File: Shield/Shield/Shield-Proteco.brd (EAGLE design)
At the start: 106.3 x 81.3 mm, 46 parts

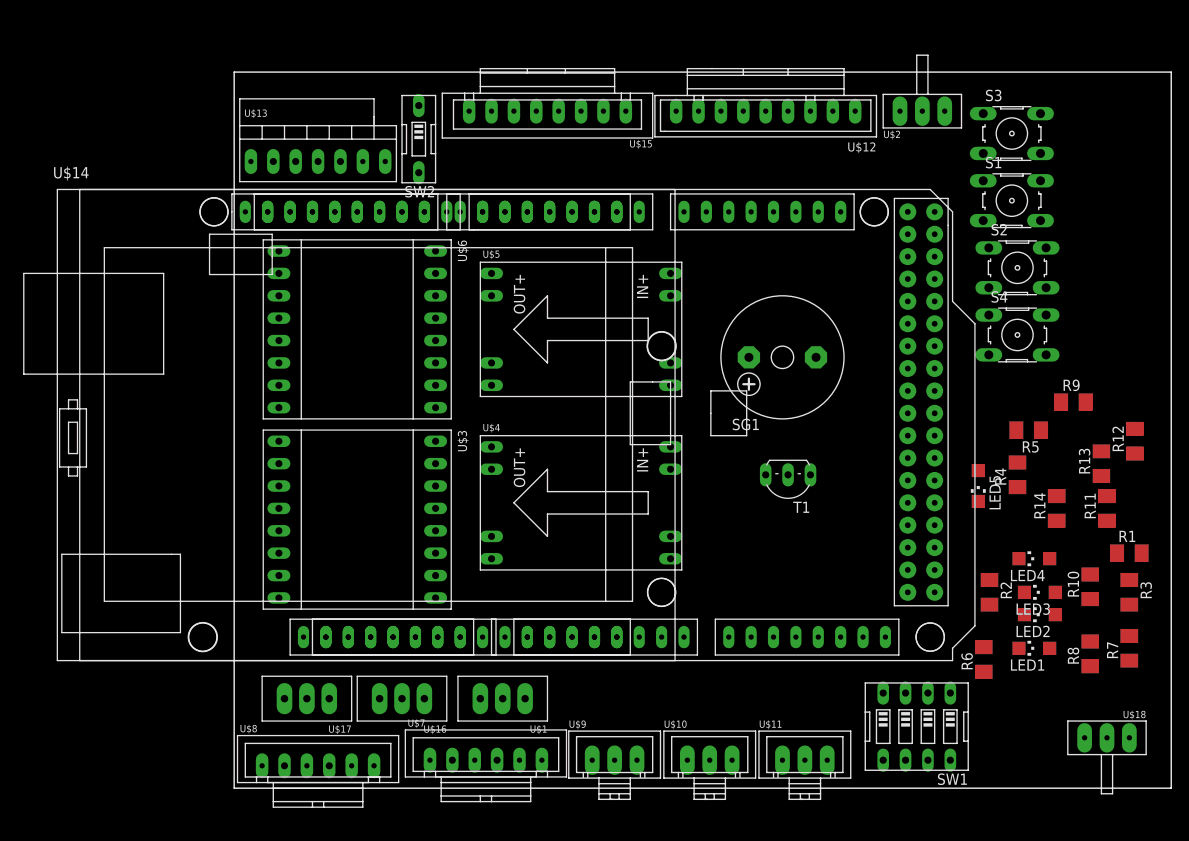
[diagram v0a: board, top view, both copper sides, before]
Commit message: Programacion Inalambrica con BT
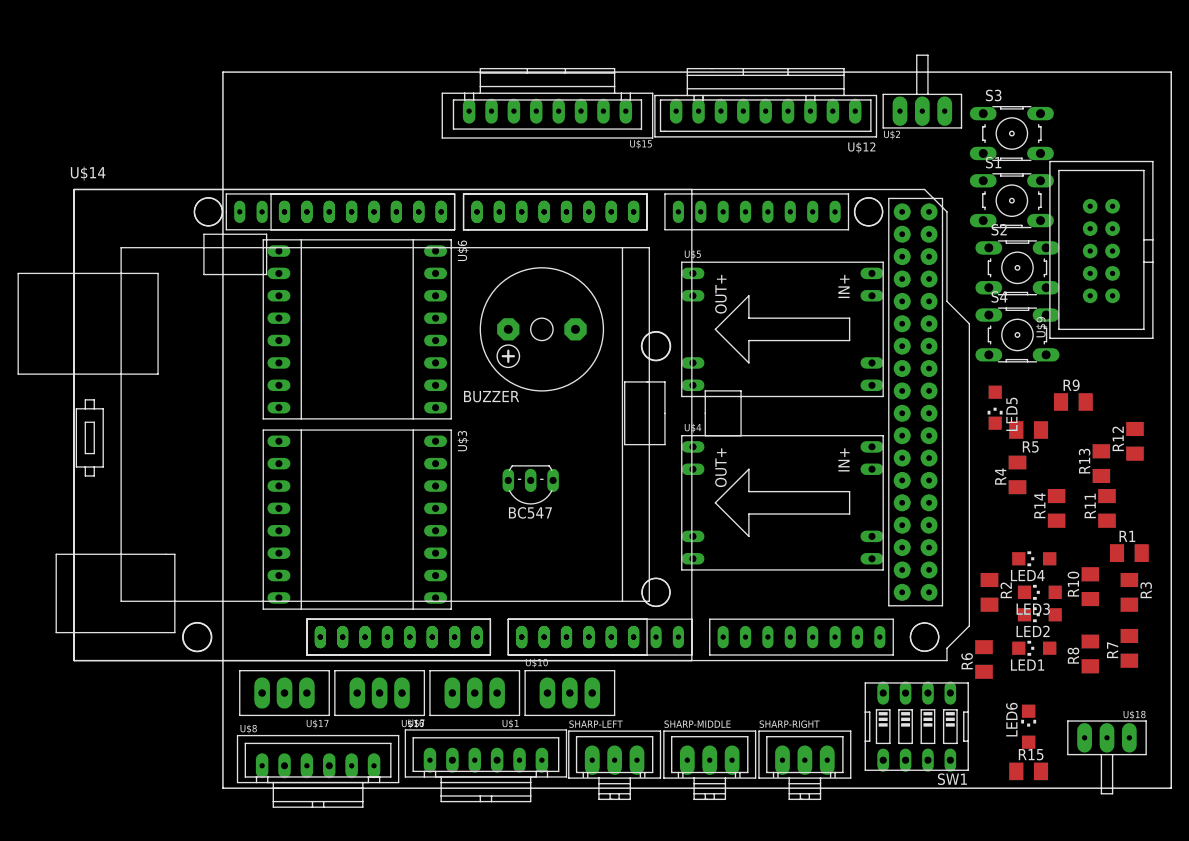
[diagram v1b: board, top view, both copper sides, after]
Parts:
- removed SG1: F/CM12P, buzzer:F/CM12P
- removed SW2: (no value), special:EDG-01
- removed T1: (no value), transistor:TO92-CBE
- removed U$13: HC-05-PROG, hc-xx:HC-05-PROG
- added BC547: (no value), transistor:TO92-CBE
- added BUZZER: F/CM12P, buzzer:F/CM12P
- added LED6: (no value), led:CHIPLED_1206
- added R15: (no value), rcl:M1206
- added SHARP-LEFT, SHARP-MIDDLE: SHARP, Sensores:SHARP
- U$10: value SHARP -> SERVOMOTORES; device Sensores:SHARP -> Motores:SERVO
- U$9: value SHARP -> SENSOR-MISCELANEOUS; device Sensores:SHARP -> Sensores:SENSOR-MISCELANEOUS
- moved U$9 79.9 mm to (98.4, 61.0), turned to 90 degrees
- moved U$4 22.9 mm to (62.2, 32.4)
- moved U$5 22.9 mm to (62.2, 52.1)
- moved U$10 17.6 mm to (38.1, 10.8)
- moved LED5 9.09 mm to (86.4, 43.2)
- moved U$1 3.24 mm to (27.3, 10.8)
- moved U$17 2.62 mm to (5.71, 10.8)
- moved U$16 2.62 mm to (16.5, 10.8)
- moved U$14 1.90 mm to (15.9, 38.7)
- moved ARDUINO-MEGA 0.64 mm to (31.1, 40.0)
- renumbered U$11 to SHARP-RIGHT
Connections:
- removed net N$16: SW2.1, U$13.RESET
- removed net RX0: U$13.RXD
- removed net TX0: U$13.TXD
- new net LED1: LED1.A
- new net LED2: LED2.A
- new net LED3: LED3.A
- new net LED4: LED4.A
- new net LED5: LED5.A
- new net N$100: U$3.AO2, U$3.BO2
- new net N$101: U$3.AO1, U$3.BO1
- new net N$102: U$7.OUTB
- new net N$103: U$7.OUTA
- new net N$104: U$7.M2
- new net N$105: U$7.M1
- new net N$106: U$8.OUTA
- new net N$107: U$8.OUTB
- new net N$108: U$8.M2
- new net N$109: U$8.M1
- new net N$110: U$9.3V3
- new net N$111: ARDUINO-MEGA.12
- new net N$112: ARDUINO-MEGA.11
- new net N$113: ARDUINO-MEGA.10
- new net N$114: ARDUINO-MEGA.9
- new net N$115: ARDUINO-MEGA.8
- new net N$116: ARDUINO-MEGA.7
- new net N$117: ARDUINO-MEGA.6
- new net N$69: U$9.1
- new net N$82: U$9.2
- new net N$83: U$9.3
- new net N$84: U$9.4
- new net N$85: U$9.5
- new net N$86: U$9.6
- new net N$87: U$9.7
- new net N$88: LED5.C, R14.2
- new net N$89: LED6.C, R15.2
- new net N$92: U$6.AI1, U$6.BI1
- new net N$93: U$6.AI2, U$6.BI2
- new net N$94: U$6.AO2, U$6.BO2
- new net N$95: U$6.AO1, U$6.BO1
- new net N$96: U$6.PWMA, U$6.PWMB
- new net N$97: U$3.AI1, U$3.BI1
- new net N$98: U$3.AI2, U$3.BI2
- new net N$99: U$3.PWMA, U$3.PWMB
- net GND: now also BC547.E, R15.1, SHARP-LEFT.GND, SHARP-MIDDLE.GND; no longer T1.E, U$13.GND
- net N$10: now also S2.4
- net N$11: now also S1.4
- net N$12: now also S3.4
- net N$13: now also S4.4
- net N$5: now also BC547.C, BUZZER.-; no longer SG1.-, T1.C
- net N$6: now also BC547.B; no longer T1.B
- net N$7: now also SHARP-LEFT.DIST; no longer U$9.DIST
- net N$77: now also U$10.SIGNAL
- net N$8: now also SHARP-MIDDLE.DIST; no longer U$10.DIST
- net RESET: no longer SW2.2
- net VCC: now also BUZZER.+, LED6.A, SHARP-LEFT.VCC, SHARP-MIDDLE.VCC; no longer SG1.+, U$13.VCC
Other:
- board size 106.3 x 81.3 mm -> 107.6 x 81.3 mm

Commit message: Más avance
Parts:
- added D1, D2, D3, D4: (no value), diode:DO-214AC
- added Q1: FDD4141TO252, transistor-fet:TO252
- added U$11: ACELEROMETER-JST-5, Sensores:ACELEROMETER-MPU6050-JST-5
- added U$13: HC-05-PROGRAMER, hc-xx:HC-05-PROG-COMP
- added U$19: SW-HEAD, Interruptores:1X02
- added U$20, U$21: FAN-MOLEX, Ventilador:1X02
- added U$22: LED-1W-3V3, LedPower:1X02
- added U$23: ZIIPY-7.4V, Baterias:XT60
- U$12: value CNY70-ARRAY -> CNY70-ARRAY-HEADER; device Sensores:CNY70-ARRAY -> Sensores:CNY70-ARRAY-HEADER
- U$15: value ACELEROMETER-MPU6050-JST -> SLIDE-3; device Sensores:ACELEROMETER-MPU6050-JST -> Interruptores:SLIDE-3
- U$18: value SLIDE-3 -> SW-HEAD; device Interruptores:SLIDE-3 -> Interruptores:1X02
- moved U$15 95.1 mm to (97.8, 3.81)
- moved U$18 33.6 mm to (66.0, 12.1), turned to 0 degrees
- moved U$12 30.4 mm to (30.5, 71.1), turned to 0 degrees
- moved LED6 5.12 mm to (85.7, 9.53)
- moved R13 5.08 mm to (93.3, 36.8)
- moved R12 4.96 mm to (98.4, 36.2), turned to 180 degrees
- moved R15 4.84 mm to (85.7, 3.81), turned to 270 degrees
- moved R9 3.81 mm to (91.4, 43.8)
- moved U$9 3.42 mm to (99.7, 64.1)
- moved LED4 1.42 mm to (91.4, 24.8)
- moved U$2 0.90 mm to (77.5, 77.5)
- moved LED1 0.90 mm to (91.4, 16.5)
- moved U$8 0.63 mm to (9.53, 3.17)
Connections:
- new net DRAIN: Q1.3
- new net GATE: Q1.1
- new net N$118: ARDUINO-MEGA.0-RX0
- new net N$119: ARDUINO-MEGA.14-TX3
- new net N$120: ARDUINO-MEGA.15-RX3
- new net N$121: ARDUINO-MEGA.16-TX2
- new net N$122: ARDUINO-MEGA.17-RX2
- new net N$123: ARDUINO-MEGA.18-TX1
- new net N$124: ARDUINO-MEGA.19-RX1
- new net N$125: ARDUINO-MEGA.20
- new net N$126: ARDUINO-MEGA.21
- new net N$127: D1.A, U$1.SIGNAL
- new net N$128: U$18.2, U$20.VCC
- new net N$129: U$9.E9
- new net N$130: U$9.E10
- new net N$131: U$9.E11
- new net N$132: U$9.E12
- new net N$133: U$9.E13
- new net N$134: U$2.P1, U$23.VCC
- new net N$16: ARDUINO-MEGA.5
- new net N$90: ARDUINO-MEGA.1-TX0
- new net N$91: U$13.RXD
- new net RX0: U$13.TXD
- new net SERVO1: D1.C
- new net SERVO2: D2.C
- new net SERVO3: D3.C
- new net SERVO4: D4.C
- new net SOURCE: Q1.2
- net GND: now also U$11.GND, U$13.GND, U$20.GND, U$21.GND, U$23.GND; no longer U$15.GND
- net N$15: now also U$19.2, U$21.VCC; no longer U$2.COM
- net N$17: now also U$11.SCL; no longer U$15.SCL
- net N$18: now also U$11.SDA; no longer U$15.SDA
- net N$19: now also ARDUINO-MEGA.4; no longer U$15.XDA
- net N$20: now also ARDUINO-MEGA.3; no longer U$15.XCL
- net N$21: now also ARDUINO-MEGA.2; no longer U$15.ADO
- net N$22: now also U$11.INT; no longer U$15.INT
- net N$29: now also U$15.P2; no longer U$18.P2
- net N$69: now also U$9.E1; no longer U$9.1
- net N$75: now also D4.A, U$10.SIGNAL; no longer U$1.SIGNAL
- net N$76: now also D3.A, U$17.SIGNAL; no longer U$16.SIGNAL
- net N$77: now also D2.A, U$16.SIGNAL; no longer U$10.SIGNAL, U$17.SIGNAL
- net N$82: now also U$9.E2; no longer U$9.2
- net N$83: now also U$9.E3; no longer U$9.3
- net N$84: now also U$9.E4; no longer U$9.4
- net N$85: now also U$9.E5; no longer U$9.5
- net N$86: now also U$9.E6; no longer U$9.6
- net N$87: now also U$9.E7; no longer U$9.7
- net RESET: now also U$13.RESET
- net VCC: now also U$11.VCC, U$13.VCC, U$15.COM, U$18.1, U$19.1; no longer U$15.VCC, U$18.COM

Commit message: Name
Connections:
- net N$39 renamed 3V3
- removed net N$41: ARDUINO-MEGA.GND_2
- net GND: now also ARDUINO-MEGA.GND_2
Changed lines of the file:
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@@
 <contactref element="U$21" pad="GND"/>
 <contactref element="U$23" pad="GND"/>
+<contactref element="ARDUINO-MEGA" pad="GND_2"/>
 <wire x1="90.04" y1="43.815" x2="100.965" y2="55.245" width="0" layer="19" extent="1-1"/>
 <wire x1="93.345" y1="35.43" x2="90.04" y2="43.815" width="0" layer="19" extent="1-1"/>
@@
 <wire x1="40.64" y1="10.795" x2="43.18" y2="3.175" width="0" layer="19" extent="1-1"/>
 <wire x1="24.765" y1="10.795" x2="40.64" y2="10.795" width="0" layer="19" extent="1-1"/>
+<wire x1="22.479" y1="17.145" x2="24.765" y2="10.795" width="0" layer="19" extent="1-1"/>
 <wire x1="22.225" y1="3.175" x2="24.765" y2="10.795" width="0" layer="19" extent="1-1"/>
-<wire x1="13.97" y1="10.795" x2="24.765" y2="10.795" width="0" layer="19" extent="1-1"/>
+<wire x1="22.86" y1="26.67" x2="22.479" y2="17.145" width="0" layer="19" extent="1-1"/>
+<wire x1="13.97" y1="10.795" x2="22.479" y2="17.145" width="0" layer="19" extent="1-1"/>
 <wire x1="3.175" y1="10.795" x2="13.97" y2="10.795" width="0" layer="19" extent="1-1"/>
 <wire x1="3.175" y1="3.175" x2="3.175" y2="10.795" width="0" layer="19" extent="1-1"/>
-<wire x1="22.86" y1="26.67" x2="24.765" y2="10.795" width="0" layer="19" extent="1-1"/>
 <wire x1="31.115" y1="34.925" x2="22.86" y2="26.67" width="0" layer="19" extent="1-1"/>
 <wire x1="22.86" y1="39.37" x2="31.115" y2="34.925" width="0" layer="19" extent="1-1"/>
@@
 <wire x1="22.86" y1="60.96" x2="22.86" y2="48.26" width="0" layer="19" extent="1-1"/>
 <wire x1="20.32" y1="71.12" x2="22.86" y2="60.96" width="0" layer="19" extent="1-1"/>
+<wire x1="29.337" y1="76.2" x2="20.32" y2="71.12" width="0" layer="19" extent="1-1"/>
 <wire x1="5.08" y1="74.93" x2="20.32" y2="71.12" width="0" layer="19" extent="1-1"/>
 <wire x1="5.08" y1="60.96" x2="5.08" y2="74.93" width="0" layer="19" extent="1-1"/>
 <wire x1="5.08" y1="39.37" x2="22.86" y2="39.37" width="0" layer="19" extent="1-1"/>
-<wire x1="29.337" y1="76.2" x2="3.175" y2="3.175" width="0" layer="19" extent="1-1"/>
 <wire x1="55.88" y1="72.771" x2="52.07" y2="48.26" width="0" layer="19" extent="1-1"/>
 </signal>
@@
 <contactref element="U$14" pad="A5"/>
 </signal>
-<signal name="N$39">
+<signal name="3V3">
 <contactref element="ARDUINO-MEGA" pad="3V3"/>
 </signal>
@@
 <contactref element="ARDUINO-MEGA" pad="5V_1"/>
 </signal>
-<signal name="N$41">
-<contactref element="ARDUINO-MEGA" pad="GND_2"/>
-</signal>
 <signal name="N$42">

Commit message: Conexiones
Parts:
- removed LED6: (no value), led:CHIPLED_1206
- removed R1, R10, R11, R12, R13, R14, R15, R2, R3, R4, R5, R6, R7, R8, R9: (no value), rcl:M1206
- removed SW1: (no value), special:EDG-04
- removed U$1, U$10, U$16, U$17: SERVOMOTORES, Motores:SERVO
- removed U$11: ACELEROMETER-JST-5, Sensores:ACELEROMETER-MPU6050-JST-5
- removed U$12: CNY70-ARRAY-HEADER, Sensores:CNY70-ARRAY-HEADER
- removed U$13: HC-05-PROGRAMER, hc-xx:HC-05-PROG-COMP
- removed U$15, U$2: SLIDE-3, Interruptores:SLIDE-3
- removed U$18: SW-HEAD, Interruptores:1X02
- removed U$22: LED-1W-3V3, LedPower:1X02
- removed U$4, U$5: STEPDOWN-DC-DC, Reguladores:STEPDOWN-DC-DC
- removed U$7, U$8: POLOLU-MICROMOTOR, Motores:JST
- added 5V-SOURCE, MOTORS-SOURCE: STEPDOWN-DC-DC, Reguladores:STEPDOWN-DC-DC
- added ADXL335-ACELEROMETER: ACELEROMETER-JST-5, Sensores:ACELEROMETER-MPU6050-JST-5
- added DIPSW: (no value), special:EDG-04
- added HC-05-PROG: HC-05-PROGRAMER, hc-xx:HC-05-PROG-COMP
- added LED-PWR: (no value), led:CHIPLED_1206
- added LED_1W: LED-1W-3V3, LedPower:1X02
- added LINE-SENSOR: CNY70-ARRAY-HEADER, Sensores:CNY70-ARRAY-HEADER
- added MOTOR_LEFT, MOTOR_RIGHT: POLOLU-MICROMOTOR, Motores:JST
- added POWER-SW, TFT-SW: SLIDE-3, Interruptores:SLIDE-3
- added R-DIP1, R-DIP2, R-DIP3, R-DIP4, R-PUSH3, RLED-1, RLED-2, RLED-3, RLED-4, RLED-5, RLED-PWR, RPUSH-2, RPUSH-4, R_BUZZ: (no value), rcl:M1206
- added SERVO_1, SERVO_2, SERVO_3, SERVO_4: SERVOMOTORES, Motores:SERVO
- added SW_FAN1: SW-HEAD, Interruptores:1X02
- moved Q1 41.4 mm to (97.2, 4.45), turned to 90 degrees
- moved BC547 26.2 mm to (43.8, 59.1), turned to 0 degrees
- moved LED5 16.7 mm to (91.4, 27.3), turned to 270 degrees
- moved U$23 12.7 mm to (10.2, 72.4), turned to 180 degrees
- moved U$9 1.42 mm to (98.4, 63.5)
- moved SHARP-LEFT 1.27 mm to (41.9, 3.17)
- moved SHARP-MIDDLE 1.27 mm to (52.7, 3.17)
- moved SHARP-RIGHT 1.27 mm to (63.5, 3.17)
- renumbered D1 to DS1, D2 to DS2, D3 to DS3, D4 to DS4, S1 to PUSH-RST, S2 to PUSH2, S3 to PUSH3, S4 to PUSH4, U$19 to SW_FAN_AUX, U$20 to FAN1, U$21 to FAN_AUX, U$3 to DRIVER-RIGHT, U$6 to DRIVER-LEFT
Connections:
- net N$32 renamed VIN
- net N$7 renamed SHARP-LEFT
- net N$70 renamed SD_DO
- net N$71 renamed SD_DI
- net N$72 renamed SD_SS
- net N$73 renamed LCD_D1
- net N$74 renamed LCD_D0
- net N$8 renamed SHARP-MIDDLE
- net N$9 renamed SHARP-RIGHT
- net N$92 renamed IN1-MOTOR-LEFT
- net N$93 renamed IN2-MOTOR-LEFT
- net N$96 renamed PWM-MOTOR-LEFT
- net N$97 renamed IN2-MOTOR-RIGHT
- net N$98 renamed IN1-MOTOR-RIGHT
- net N$99 renamed PWM-MOTOR-RIGHT
- removed net N$1: R1.2, SW1.1
- removed net N$10: PUSH2.3, PUSH2.4, R7.2
- removed net N$100: DRIVER-RIGHT.AO2, DRIVER-RIGHT.BO2
- removed net N$101: DRIVER-RIGHT.AO1, DRIVER-RIGHT.BO1
- removed net N$102: U$7.OUTB
- removed net N$103: U$7.OUTA
- removed net N$106: U$8.OUTA
- removed net N$107: U$8.OUTB
- removed net N$11: PUSH-RST.3, PUSH-RST.4, R6.2
- removed net N$110: U$9.3V3
- removed net N$116: ARDUINO-MEGA.7
- removed net N$117: ARDUINO-MEGA.6
- removed net N$118: ARDUINO-MEGA.0-RX0
- removed net N$12: PUSH3.3, PUSH3.4, R8.2
- removed net N$13: PUSH4.3, PUSH4.4, R9.2
- removed net N$16: ARDUINO-MEGA.5
- removed net N$17: U$11.SCL
- removed net N$18: U$11.SDA
- removed net N$19: ARDUINO-MEGA.4
- removed net N$2: R2.2, SW1.2
- removed net N$20: ARDUINO-MEGA.3
- removed net N$21: ARDUINO-MEGA.2
- removed net N$22: U$11.INT
- removed net N$27: U$14.0-RX0
- removed net N$28: U$14.3V3
- removed net N$3: R3.2, SW1.3
- removed net N$33: U$14.A0
- removed net N$34: U$14.A1
- removed net N$35: U$14.A2
- removed net N$36: U$14.A3
- removed net N$37: U$14.A4
- removed net N$4: R4.2, SW1.4
- removed net N$44: ARDUINO-MEGA.A0
- removed net N$45: ARDUINO-MEGA.A1
- removed net N$46: ARDUINO-MEGA.A2
- removed net N$47: ARDUINO-MEGA.A3
- removed net N$48: ARDUINO-MEGA.A4
- removed net N$60: U$14.1-TX0
- removed net N$61: U$14.2
- removed net N$62: U$14.3
- removed net N$63: U$14.4
- removed net N$64: U$14.5
- removed net N$65: U$14.6
- removed net N$66: U$14.7
- removed net N$68: U$14.GND
- removed net N$78: ARDUINO-MEGA.SCL
- removed net N$79: ARDUINO-MEGA.SDA
- removed net N$81: ARDUINO-MEGA.GND
- removed net N$90: ARDUINO-MEGA.1-TX0
- removed net N$91: U$13.RXD
- removed net N$94: DRIVER-LEFT.AO2, DRIVER-LEFT.BO2
- removed net N$95: DRIVER-LEFT.AO1, DRIVER-LEFT.BO1
- new net DIP1: DIPSW.1, R-DIP1.2
- new net DIP2: DIPSW.2, R-DIP2.2
- new net DIP3: DIPSW.3, R-DIP3.2
- new net DIP4: DIPSW.4, R-DIP4.2
- new net INT: ADXL335-ACELEROMETER.INT
- new net LCD_CS: ARDUINO-MEGA.A3, U$14.A3
- new net LCD_D2: ARDUINO-MEGA.2, U$14.2
- new net LCD_D3: ARDUINO-MEGA.3, U$14.3
- new net LCD_D4: ARDUINO-MEGA.4, U$14.4
- new net LCD_D5: ARDUINO-MEGA.5, U$14.5
- new net LCD_D6: ARDUINO-MEGA.6, U$14.6
- new net LCD_D7: ARDUINO-MEGA.7, U$14.7
- new net LCD_RD: ARDUINO-MEGA.A0, U$14.A0
- new net LCD_RS: ARDUINO-MEGA.A2, U$14.A2
- new net LCD_RST: ARDUINO-MEGA.A4, U$14.A4
- new net LCD_WR: ARDUINO-MEGA.A1, U$14.A1
- new net OUT1-MOTOR-LEFT: DRIVER-LEFT.AO1, DRIVER-LEFT.BO1, MOTOR_LEFT.OUTB
- new net OUT1-MOTOR-RIGHT: DRIVER-RIGHT.AO1, DRIVER-RIGHT.BO1, MOTOR_RIGHT.OUTB
- new net OUT2-MOTOR-LEFT: DRIVER-LEFT.AO2, DRIVER-LEFT.BO2, MOTOR_LEFT.OUTA
- new net OUT2-MOTOR-RIGHT: DRIVER-RIGHT.AO2, DRIVER-RIGHT.BO2, MOTOR_RIGHT.OUTA
- new net PUSH2: PUSH2.3, PUSH2.4, RPUSH-2.2
- new net PUSH3: PUSH3.3, PUSH3.4, R-PUSH3.2
- new net PUSH4: PUSH4.3, PUSH4.4, RPUSH-4.2
- new net SCL: ADXL335-ACELEROMETER.SCL, ARDUINO-MEGA.SCL
- new net SDA: ADXL335-ACELEROMETER.SDA, ARDUINO-MEGA.SDA
- new net TX0: ARDUINO-MEGA.1-TX0, HC-05-PROG.RXD, U$14.1-TX0
- net 3V3: now also U$14.3V3, U$9.3V3
- net 6V-DC-3A: now also MOTORS-SOURCE.OUT+; no longer U$5.OUT+
- net BUZZER: now also R_BUZZ.1; no longer R5.1
- net GND: now also 5V-SOURCE.IN-, 5V-SOURCE.OUT-, ADXL335-ACELEROMETER.GND, ARDUINO-MEGA.GND, HC-05-PROG.GND, LINE-SENSOR.GND, MOTORS-SOURCE.IN-, MOTORS-SOURCE.OUT-, MOTOR_LEFT.GND, MOTOR_RIGHT.GND, R-DIP1.1, R-DIP2.1, R-DIP3.1, R-DIP4.1, R-PUSH3.1, RLED-1.1, RLED-2.1, RLED-3.1, RLED-4.1, RLED-5.1, RLED-PWR.1, RPUSH-2.1, RPUSH-4.1, SERVO_1.GND, SERVO_2.GND, SERVO_3.GND, SERVO_4.GND, U$14.GND; no longer R1.1, R10.1, R11.1, R12.1, R13.1, R14.1, R15.1, R2.1, R3.1, R4.1, R6.1, R7.1, R8.1, R9.1, U$1.GND, U$10.GND, U$11.GND, U$12.GND, U$13.GND, U$16.GND, U$17.GND, U$4.IN-, U$4.OUT-, U$5.IN-, U$5.OUT-, U$7.GND, U$8.GND
- net N$104: now also MOTOR_LEFT.M2; no longer U$7.M2
- net N$105: now also MOTOR_LEFT.M1; no longer U$7.M1
- net N$108: now also MOTOR_RIGHT.M2; no longer U$8.M2
- net N$109: now also MOTOR_RIGHT.M1; no longer U$8.M1
- net N$127: now also SERVO_1.SIGNAL; no longer U$1.SIGNAL
- net N$128: now also SW_FAN1.2; no longer U$18.2
- net N$134: now also POWER-SW.P1; no longer U$2.P1
- net N$14: now also 5V-SOURCE.IN+, MOTORS-SOURCE.IN+, POWER-SW.P2; no longer U$2.P2, U$4.IN+, U$5.IN+
- net N$23: now also RLED-1.2; no longer R10.2
- net N$24: now also RLED-2.2; no longer R11.2
- net N$25: now also RLED-3.2; no longer R12.2
- net N$26: now also RLED-4.2; no longer R13.2
- net N$29: now also TFT-SW.P2; no longer U$15.P2
- net N$6: now also R_BUZZ.2; no longer R5.2
- net N$75: now also SERVO_4.SIGNAL; no longer U$10.SIGNAL
- net N$76: now also SERVO_3.SIGNAL; no longer U$17.SIGNAL
- net N$77: now also SERVO_2.SIGNAL; no longer U$16.SIGNAL
- net N$88: now also RLED-5.2; no longer R14.2
- net N$89: now also LED-PWR.C, RLED-PWR.2; no longer LED6.C, R15.2
- net RESET: now also HC-05-PROG.RESET, PUSH-RST.3, PUSH-RST.4; no longer U$13.RESET
- net RX0: now also ARDUINO-MEGA.0-RX0, HC-05-PROG.TXD, U$14.0-RX0; no longer U$13.TXD
- net SCD: now also LINE-SENSOR.SCD; no longer U$12.SCD
- net SCI: now also LINE-SENSOR.SCI; no longer U$12.SCI
- net SF: now also LINE-SENSOR.SF; no longer U$12.SF
- net SID: now also LINE-SENSOR.SID; no longer U$12.SID
- net SII: now also LINE-SENSOR.SII; no longer U$12.SII
- net SSD: now also LINE-SENSOR.SSD; no longer U$12.SSD
- net SSI: now also LINE-SENSOR.SSI; no longer U$12.SSI
- net VCC: now also 5V-SOURCE.OUT+, ADXL335-ACELEROMETER.VCC, DIPSW.5, DIPSW.6, DIPSW.7, DIPSW.8, HC-05-PROG.VCC, LED-PWR.A, LINE-SENSOR.VCC, MOTOR_LEFT.VCC, MOTOR_RIGHT.VCC, SERVO_1.VCC, SERVO_2.VCC, SERVO_3.VCC, SERVO_4.VCC, SW_FAN1.1, TFT-SW.COM; no longer LED6.A, SW1.5, SW1.6, SW1.7, SW1.8, U$1.VCC, U$10.VCC, U$11.VCC, U$12.VCC, U$13.VCC, U$15.COM, U$16.VCC, U$17.VCC, U$18.1, U$4.OUT+, U$7.VCC, U$8.VCC

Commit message: Conexiones+
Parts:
- removed TFT-SW: SLIDE-3, Interruptores:SLIDE-3
- moved Q1 78.1 mm to (62.2, 74.3), turned to 0 degrees
- moved MOTORS-SOURCE 53.0 mm to (11.4, 37.5)
- moved U$9 49.6 mm to (87.0, 15.2)
- moved DS1 42.3 mm to (4.45, 15.9), turned to 0 degrees
- moved FAN1 38.8 mm to (54.6, 11.4), turned to 270 degrees
- moved FAN_AUX 38.8 mm to (59.7, 11.4), turned to 270 degrees
- moved RPUSH-2 36.4 mm to (88.3, 51.4)
- moved 5V-SOURCE 34.9 mm to (11.4, 53.3)
- moved R-PUSH3 34.8 mm to (91.4, 51.4)
- moved BC547 33.4 mm to (55.9, 27.9)
- moved RPUSH-4 31.9 mm to (84.5, 51.4)
- moved BUZZER 28.5 mm to (59.1, 36.8), turned to 90 degrees
- moved LED-PWR 27.7 mm to (90.8, 31.8), turned to 90 degrees
- moved RLED-PWR 25.8 mm to (84.5, 29.8), turned to 0 degrees
- moved LINE-SENSOR 24.8 mm to (69.8, 43.8), turned to 90 degrees
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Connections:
- removed net N$111: ARDUINO-MEGA.12
- removed net N$112: ARDUINO-MEGA.11
- removed net N$113: ARDUINO-MEGA.10
- removed net N$114: ARDUINO-MEGA.9
- removed net N$115: ARDUINO-MEGA.8
- removed net N$29: TFT-SW.P2, U$14.5V_1
- removed net N$30: U$14.GND_2
- removed net N$31: U$14.GND_1
- removed net N$40: ARDUINO-MEGA.5V_1
- removed net N$42: ARDUINO-MEGA.GND_1
- removed net N$43: ARDUINO-MEGA.VIN
- removed net N$67: U$14.AREF
- removed net N$80: ARDUINO-MEGA.AREF
- new net AREF: ARDUINO-MEGA.AREF, U$14.AREF
- net GND: now also ARDUINO-MEGA.GND_1, U$14.GND_1, U$14.GND_2
- net LCD_D0: now also ARDUINO-MEGA.8
- net LCD_D1: now also ARDUINO-MEGA.9
- net N$134: now also POWER-SW.COM; no longer POWER-SW.P1
- net SD_DI: now also ARDUINO-MEGA.11
- net SD_DO: now also ARDUINO-MEGA.12
- net SD_SS: now also ARDUINO-MEGA.10
- net VCC: now also ARDUINO-MEGA.5V_1, U$14.5V_1; no longer TFT-SW.COM
- net VIN: now also ARDUINO-MEGA.VIN
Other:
- board size 107.6 x 81.3 mm -> 98.7 x 81.3 mm

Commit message: Disposicion de pines
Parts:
- removed LED5: (no value), led:CHIPLED_1206
- removed PUSH3, PUSH4: (no value), switch-omron:B3F-10XX
- removed R-PUSH3, RLED-5, RPUSH-4: (no value), rcl:M1206
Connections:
- removed net LED5: LED5.A
- removed net N$88: LED5.C, RLED-5.2
- removed net PUSH3: PUSH3.3, PUSH3.4, R-PUSH3.2
- removed net PUSH4: PUSH4.3, PUSH4.4, RPUSH-4.2
- new net N$1: U$9.E8
- net GND: no longer R-PUSH3.1, RLED-5.1, RPUSH-4.1
- net VCC: no longer PUSH3.1, PUSH4.1
